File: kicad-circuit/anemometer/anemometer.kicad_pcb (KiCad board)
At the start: 2 copper layers, 152.4 x 76.2 mm, 55 parts, among them J5VIN1 Conn_01x03, J5VIN2 Conn_01x03, Q1 TIP41, Q2 2N3906, U1 LM358, U2 LM324

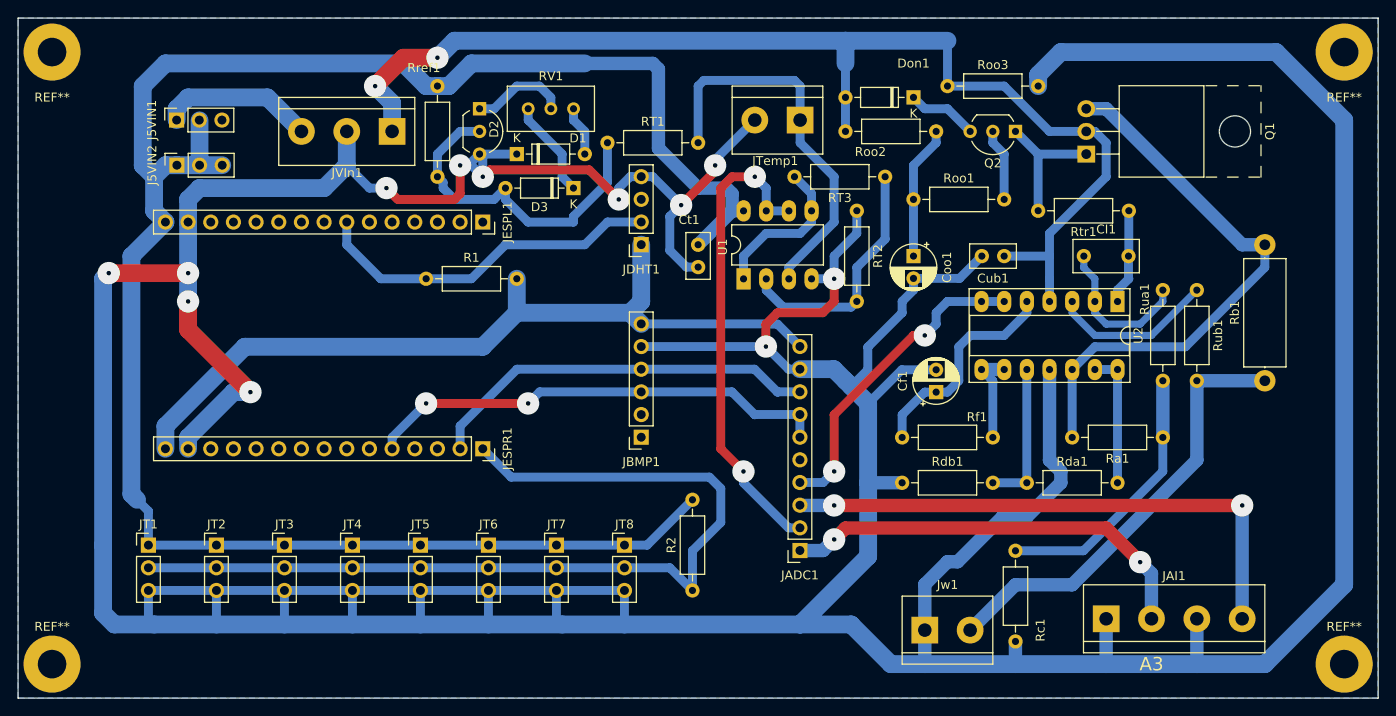
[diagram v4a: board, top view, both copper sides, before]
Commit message: Working on wifi
COuldn't do anything besides connecting to the wifi router.
Still figuring things out. This code is crap, just for experimenting.
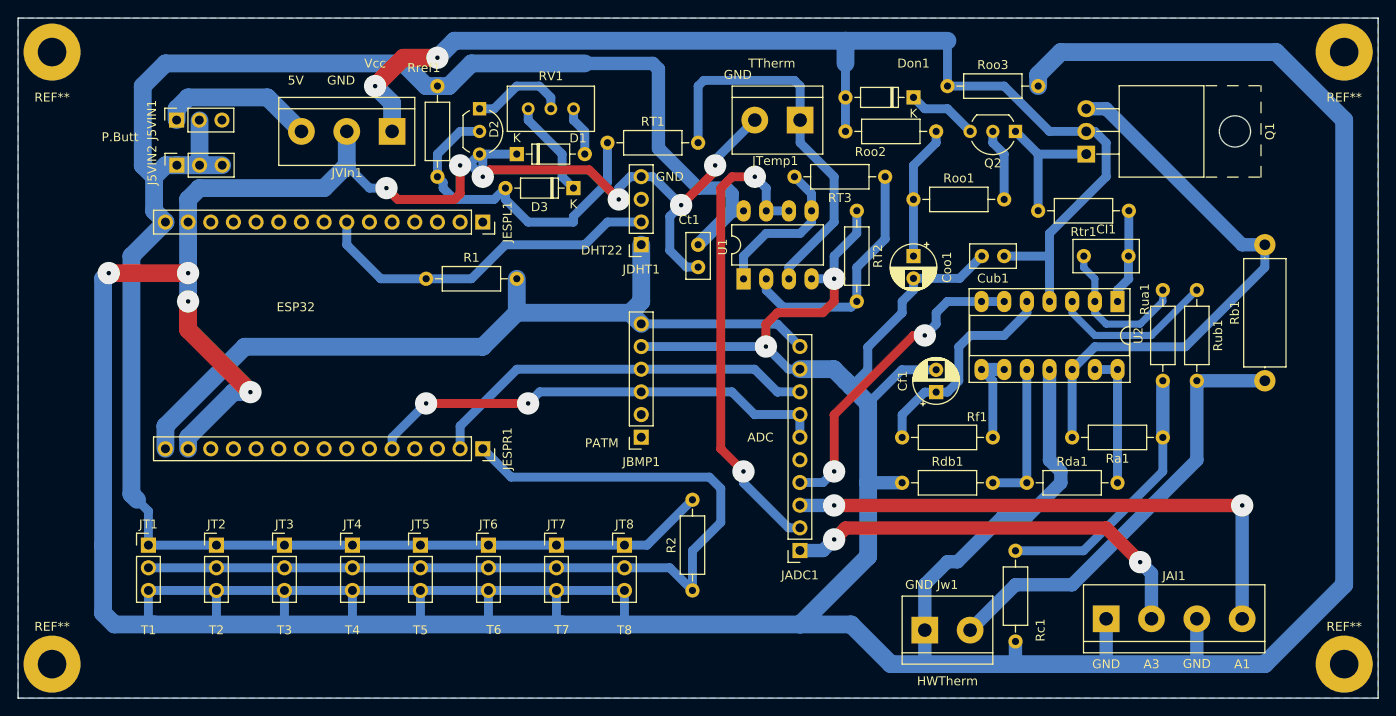
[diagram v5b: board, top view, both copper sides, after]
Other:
- board text added: "5V"
- board text added: "A1"
- board text added: "ADC"
- board text added: "DHT22"
- board text added: "ESP32"
- board text added: "GND"
- board text added: "HWTherm"
- board text added: "P.Butt"
- board text added: "PATM"
- board text added: "T1"
- board text added: "T2"
- board text added: "T3"
- board text added: "T4"
- board text added: "T5"
- board text added: "T6"
- board text added: "T7"
- board text added: "T8"
- board text added: "TTherm"
- board text added: "Vcc"
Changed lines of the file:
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@@
       (layerselection 0x00010fc_ffffffff)
       (disableapertmacros false)
-      (usegerberextensions false)
-      (usegerberattributes true)
-      (usegerberadvancedattributes true)
-      (creategerberjobfile true)
+      (usegerberextensions true)
+      (usegerberattributes false)
+      (usegerberadvancedattributes false)
+      (creategerberjobfile false)
       (svguseinch false)
       (svgprecision 6)
@@
       (psa4output false)
       (plotreference true)
-      (plotvalue true)
+      (plotvalue false)
       (plotinvisibletext false)
       (sketchpadsonfab false)
-      (subtractmaskfromsilk false)
+      (subtractmaskfromsilk true)
       (outputformat 1)
       (mirror false)
-      (drillshape 1)
+      (drillshape 0)
       (scaleselection 1)
-      (outputdirectory "")
+      (outputdirectory "../gerber/")
     )
   )
@@
   )
   (gr_rect (start 76.2 38.1) (end 228.6 114.3) (layer "Edge.Cuts") (width 0.05) (fill none))
+  (gr_text "GND" (at 156.845 44.45) (layer "F.SilkS")
+    (effects (font (size 1 1) (thickness 0.15)))
+  )
+  (gr_text "GND" (at 149.225 55.88) (layer "F.SilkS")
+    (effects (font (size 1 1) (thickness 0.15)))
+  )
+  (gr_text "GND" (at 208.28 110.452038) (layer "F.SilkS")
+    (effects (font (size 1 1) (thickness 0.15)))
+  )
+  (gr_text "ESP32" (at 107.315 70.485) (layer "F.SilkS")
+    (effects (font (size 1 1) (thickness 0.15)))
+  )
+  (gr_text "5V" (at 107.315 45.085) (layer "F.SilkS")
+    (effects (font (size 1 1) (thickness 0.15)))
+  )
+  (gr_text "ADC" (at 159.385 85.09) (layer "F.SilkS")
+    (effects (font (size 1 1) (thickness 0.15)))
+  )
+  (gr_text "T4" (at 113.665 106.68) (layer "F.SilkS")
+    (effects (font (size 1 1) (thickness 0.15)))
+  )
+  (gr_text "P.Butt" (at 87.63 51.435) (layer "F.SilkS")
+    (effects (font (size 1 1) (thickness 0.15)))
+  )
+  (gr_text "TTherm" (at 160.655 43.18) (layer "F.SilkS")
+    (effects (font (size 1 1) (thickness 0.15)))
+  )
+  (gr_text "GND" (at 198.12 110.49) (layer "F.SilkS")
+    (effects (font (size 1 1) (thickness 0.15)))
+  )
+  (gr_text "T8" (at 144.145 106.68) (layer "F.SilkS")
+    (effects (font (size 1 1) (thickness 0.15)))
+  )
+  (gr_text "Vcc" (at 116.205 43.18) (layer "F.SilkS")
+    (effects (font (size 1 1) (thickness 0.15)))
+  )
   (gr_text "A3" (at 203.2 110.49) (layer "F.SilkS")
-    (effects (font (size 1.5 1.5) (thickness 0.3)))
+    (effects (font (size 1 1) (thickness 0.15)))
+  )
+  (gr_text "GND" (at 112.395 45.085) (layer "F.SilkS")
+    (effects (font (size 1 1) (thickness 0.15)))
+  )
+  (gr_text "A1\n" (at 213.36 110.49) (layer "F.SilkS")
+    (effects (font (size 1 1) (thickness 0.15)))
+  )
+  (gr_text "T6" (at 129.513959 106.650718) (layer "F.SilkS")
+    (effects (font (size 1 1) (thickness 0.15)))
+  )
+  (gr_text "GND" (at 177.165 101.6) (layer "F.SilkS")
+    (effects (font (size 1 1) (thickness 0.15)))
+  )
+  (gr_text "T1" (at 90.805 106.68) (layer "F.SilkS")
+    (effects (font (size 1 1) (thickness 0.15)))
+  )
+  (gr_text "T5" (at 121.285 106.68) (layer "F.SilkS")
+    (effects (font (size 1 1) (thickness 0.15)))
+  )
+  (gr_text "DHT22" (at 141.605 64.135) (layer "F.SilkS")
+    (effects (font (size 1 1) (thickness 0.15)))
+  )
+  (gr_text "PATM" (at 141.605 85.725) (layer "F.SilkS")
+    (effects (font (size 1 1) (thickness 0.15)))
+  )
+  (gr_text "T3" (at 106.045 106.68) (layer "F.SilkS")
+    (effects (font (size 1 1) (thickness 0.15)))
+  )
+  (gr_text "T2" (at 98.425 106.68) (layer "F.SilkS")
+    (effects (font (size 1 1) (thickness 0.15)))
+  )
+  (gr_text "HWTherm" (at 180.34 112.395) (layer "F.SilkS")
+    (effects (font (size 1 1) (thickness 0.15)))
+  )
+  (gr_text "T7" (at 137.127449 106.650718) (layer "F.SilkS")
+    (effects (font (size 1 1) (thickness 0.15)))
   )
   (segment (start 128.27 74.93) (end 132.08 71.12) (width 2) (layer "B.Cu") (net 1))
